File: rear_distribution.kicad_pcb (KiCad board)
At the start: 4 copper layers, 210 x 100 mm, 130 parts, among them J1 Conn_01x06, J11 Conn_01x35, J2 Conn_01x06, J21 Conn_01x23, J3 47219-2001, J31 Conn_01x23, J41 Conn_01x23, J51 Conn_01x08, J61 Conn_01x08, J71 Conn_01x02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

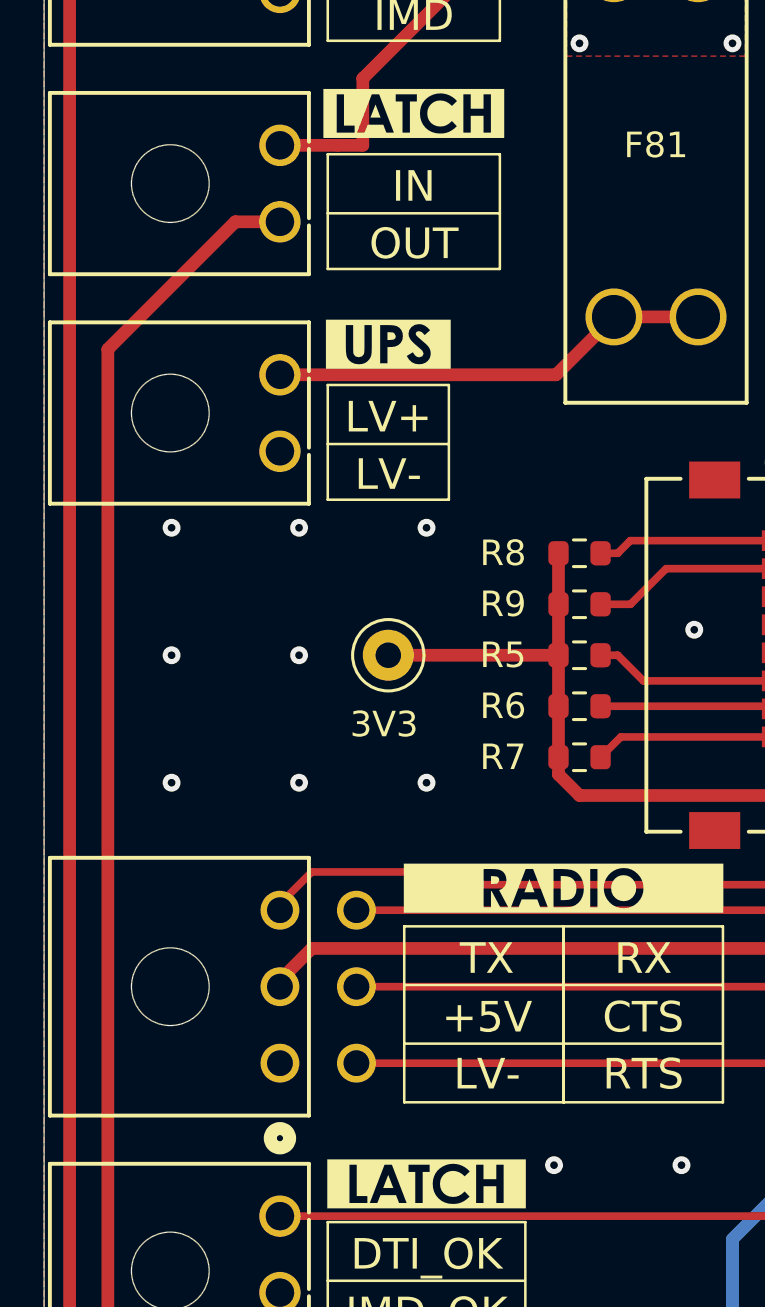
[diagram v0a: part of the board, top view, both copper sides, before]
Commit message: pcb: Add model for 2x3 MF+ and fix fuse model alignment
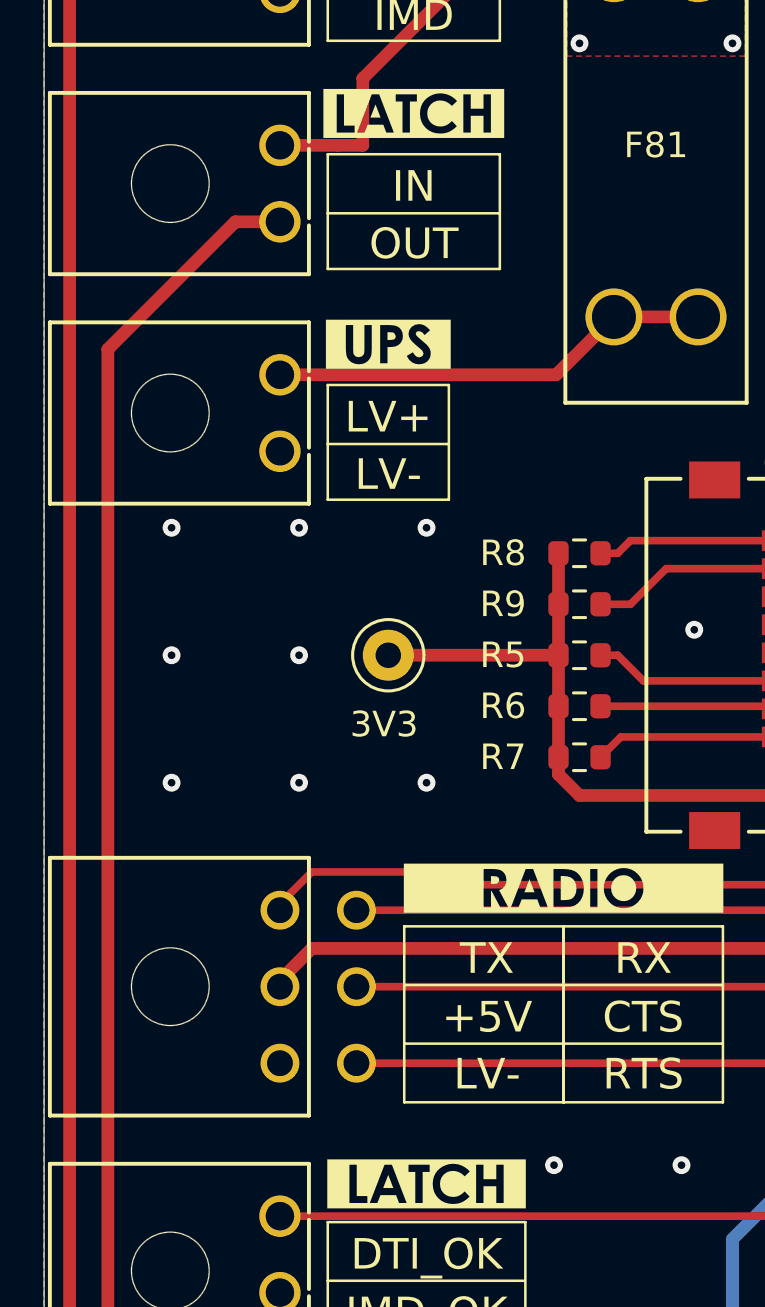
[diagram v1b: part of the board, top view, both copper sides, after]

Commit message: *: Add CAN test points
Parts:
- added CANH: TestPoint, TestPoint:TestPoint_THTPad_D2.0mm_Drill1.0mm, F.Cu at (217.0, 100.5)
- added CANL: TestPoint, TestPoint:TestPoint_THTPad_D2.0mm_Drill1.0mm, F.Cu at (213.0, 100.5)
- renumbered TP6 to TP1, TP1 to TP2, TP2 to TP3
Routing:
- net 12V_BMS: track 93.5 -> 97.4 mm

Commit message: pcb: Cleanup silkscreen some more
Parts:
- removed kibuzzard-6A356FF1: G***, kibuzzard-6A356FF1
- removed kibuzzard-6A357015 (x2): G***, kibuzzard-6A357015
- removed kibuzzard-6A357544: G***, kibuzzard-6A357544
- added kibuzzard-6910BB45: G***, kibuzzard-6910BB45, F.Cu at (128.0, 92.0)
- added kibuzzard-6A35CDBD: G***, kibuzzard-6A35CDBD, F.Cu at (236.5, 57.5)
- added kibuzzard-6A35CEAD: G***, kibuzzard-6A35CEAD, F.Cu at (235.5, 63.9)
- added kibuzzard-6A35CF3E: G***, kibuzzard-6A35CF3E, F.Cu at (55.0, 70.0)
- added kibuzzard-6A35CF3E: G***, kibuzzard-6A35CF3E, F.Cu at (55.0, 78.9)
- added kibuzzard-6A35CF98: G***, kibuzzard-6A35CF98, F.Cu at (55.0, 88.0)
- moved kibuzzard-6940937D 0.20 mm to (233.8, 108.9)
- moved kibuzzard-6A35710C 0.20 mm to (55.0, 120.9)
- moved kibuzzard-6A3572FA 0.20 mm to (235.0, 72.9)
- moved kibuzzard-6A3574B6 0.20 mm to (233.8, 96.9)
- moved kibuzzard-6A35750C 0.10 mm to (235.0, 87.9)
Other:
- board text added: "BMS_IND"
- board text added: "IMD_IND"
- board text added: "SDN_IN"
- board text added: "SDN_OUT"
- board text removed: "BMS"
- board text removed: "IMD"
- board text removed: "IN"
